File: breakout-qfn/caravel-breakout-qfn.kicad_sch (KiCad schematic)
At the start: 16 parts, among them CON1 REF-182665-01, CON2 REF-182665-01, CON3 73251-1352, U1 Caravel_QFN, U2 TLV73318PDBV

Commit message: v2.0
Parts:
- removed C8, C9: 0.1uf, Capacitor_SMD:C_0603_1608Metric, symbol Device:C
- removed U2: TLV73318PDBV, Package_TO_SOT_SMD:SOT-23-5, symbol Regulator_Linear:TLV73318PDBV
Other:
- title: (none) -> Caravel QFN Breakout
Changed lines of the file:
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@@
 (kicad_sch (version 20230121) (generator eeschema)
   (paper "A")
+  (title_block
+    (title "Caravel QFN Breakout")
+    (date "2023-07-17")
+    (rev "2.0")
+  )
   (junction (at 41.91 93.98) (diameter 0) (color 0 0 0 0)
   )
@@
     )
   )
-  (symbol (lib_id "Device:C") (at 161.29 156.21 180) (unit 1)
-    (in_bom yes) (on_board yes) (dnp no)
-    (property "Reference" "C9" (at 157.48 156.21 90)
-      (effects (font (size 1.27 1.27)))
-    )
-    (property "Value" "0.1uf" (at 154.94 156.21 90)
-      (effects (font (size 1.27 1.27)))
-    )
-    (property "Footprint" "Capacitor_SMD:C_0603_1608Metric" (at 160.3248 152.4 0)
-      (effects (font (size 1.27 1.27)) hide)
-    )
-    (property "Datasheet" "~" (at 161.29 156.21 0)
-      (effects (font (size 1.27 1.27)) hide)
-    )
-    (pin "1")
-    (pin "2")
-    (instances
-      (project "caravel-breakout-qfn"
-        (path "/b38c65ac-2d57-46f9-9a32-ad09573ee400"
-          (reference "C9") (unit 1)
-        )
-      )
-    )
-  )
-  (symbol (lib_id "Regulator_Linear:TLV73318PDBV") (at 146.05 154.94 0) (unit 1)
-    (in_bom yes) (on_board yes) (dnp no) (fields_autoplaced)
-    (property "Reference" "U2" (at 146.05 144.78 0)
-      (effects (font (size 1.27 1.27)))
-    )
-    (property "Value" "TLV73318PDBV" (at 146.05 147.32 0)
-      (effects (font (size 1.27 1.27)))
-    )
-    (property "Footprint" "Package_TO_SOT_SMD:SOT-23-5" (at 146.05 146.685 0)
-      (effects (font (size 1.27 1.27) italic) hide)
-    )
-    (property "Datasheet" "http://www.ti.com/lit/ds/symlink/tlv733p.pdf" (at 146.05 154.94 0)
-      (effects (font (size 1.27 1.27)) hide)
-    )
-    (pin "1")
-    (pin "2")
-    (pin "3")
-    (pin "4")
-    (pin "5")
-    (instances
-      (project "caravel-breakout-qfn"
-        (path "/b38c65ac-2d57-46f9-9a32-ad09573ee400"
-          (reference "U2") (unit 1)
-        )
-      )
-    )
-  )
   (symbol (lib_id "power:GND") (at 72.39 114.3 0) (unit 1)
     (in_bom yes) (on_board yes) (dnp no)
@@
         )
       )
-    )
-  )
-  (symbol (lib_id "Device:C") (at 130.81 156.21 180) (unit 1)
-    (in_bom yes) (on_board yes) (dnp no)
-    (property "Reference" "C8" (at 127 156.21 90)
-      (effects (font (size 1.27 1.27)))
-    )
-    (property "Value" "0.1uf" (at 124.46 156.21 90)
-      (effects (font (size 1.27 1.27)))
-    )
-    (property "Footprint" "Capacitor_SMD:C_0603_1608Metric" (at 129.8448 152.4 0)
-      (effects (font (size 1.27 1.27)) hide)
-    )
-    (property "Datasheet" "~" (at 130.81 156.21 0)
-      (effects (font (size 1.27 1.27)) hide)
-    )
-    (pin "1")
-    (pin "2")
-    (instances
-      (project "caravel-breakout-qfn"
-        (path "/b38c65ac-2d57-46f9-9a32-ad09573ee400"
-          (reference "C8") (unit 1)
-        )
-      )

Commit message: QFN breakout v2.1: fixes to footprint s.masks, cleanup, flipped logos
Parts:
- CON1, CON2: footprint ok-connectors:REF-182665-01 -> BreakoutCommon:REF-182665-01
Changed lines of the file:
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@@
   (title_block
     (title "Caravel QFN Breakout")
-    (date "2023-07-17")
-    (rev "2.0")
+    (date "2023-07-21")
+    (rev "2.1")
   )
   (junction (at 41.91 93.98) (diameter 0) (color 0 0 0 0)
@@
       (effects (font (size 1.27 1.27)))
     )
-    (property "Footprint" "ok-connectors:REF-182665-01" (at 222.25 52.07 0)
+    (property "Footprint" "BreakoutCommon:REF-182665-01" (at 222.25 52.07 0)
       (effects (font (size 1.27 1.27)) hide)
     )
@@
       (effects (font (size 1.27 1.27)))
     )
-    (property "Footprint" "ok-connectors:REF-182665-01" (at 222.25 125.73 0)
-      (effects (font (size 1.27 1.27)) hide)
-    )
+    (property "Footprint" "BreakoutCommon:REF-182665-01" (at 222.25 125.73 0)
+      (effects (font (size 1.27 1.27)) hide)
+    )

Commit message: QFN v2.2, using cheaper FH-00339 headers
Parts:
- CON1, CON2: footprint BreakoutCommon:REF-182665-01 -> BreakoutCommon:FH-00339
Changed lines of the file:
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@@
       (effects (font (size 1.27 1.27)))
     )
-    (property "Footprint" "BreakoutCommon:REF-182665-01" (at 222.25 52.07 0)
+    (property "Footprint" "BreakoutCommon:FH-00339" (at 222.25 52.07 0)
       (effects (font (size 1.27 1.27)) hide)
     )
@@
       (effects (font (size 1.27 1.27)))
     )
-    (property "Footprint" "BreakoutCommon:REF-182665-01" (at 222.25 125.73 0)
-      (effects (font (size 1.27 1.27)) hide)
-    )
+    (property "Footprint" "BreakoutCommon:FH-00339" (at 222.25 125.73 0)
+      (effects (font (size 1.27 1.27)) hide)
+    )

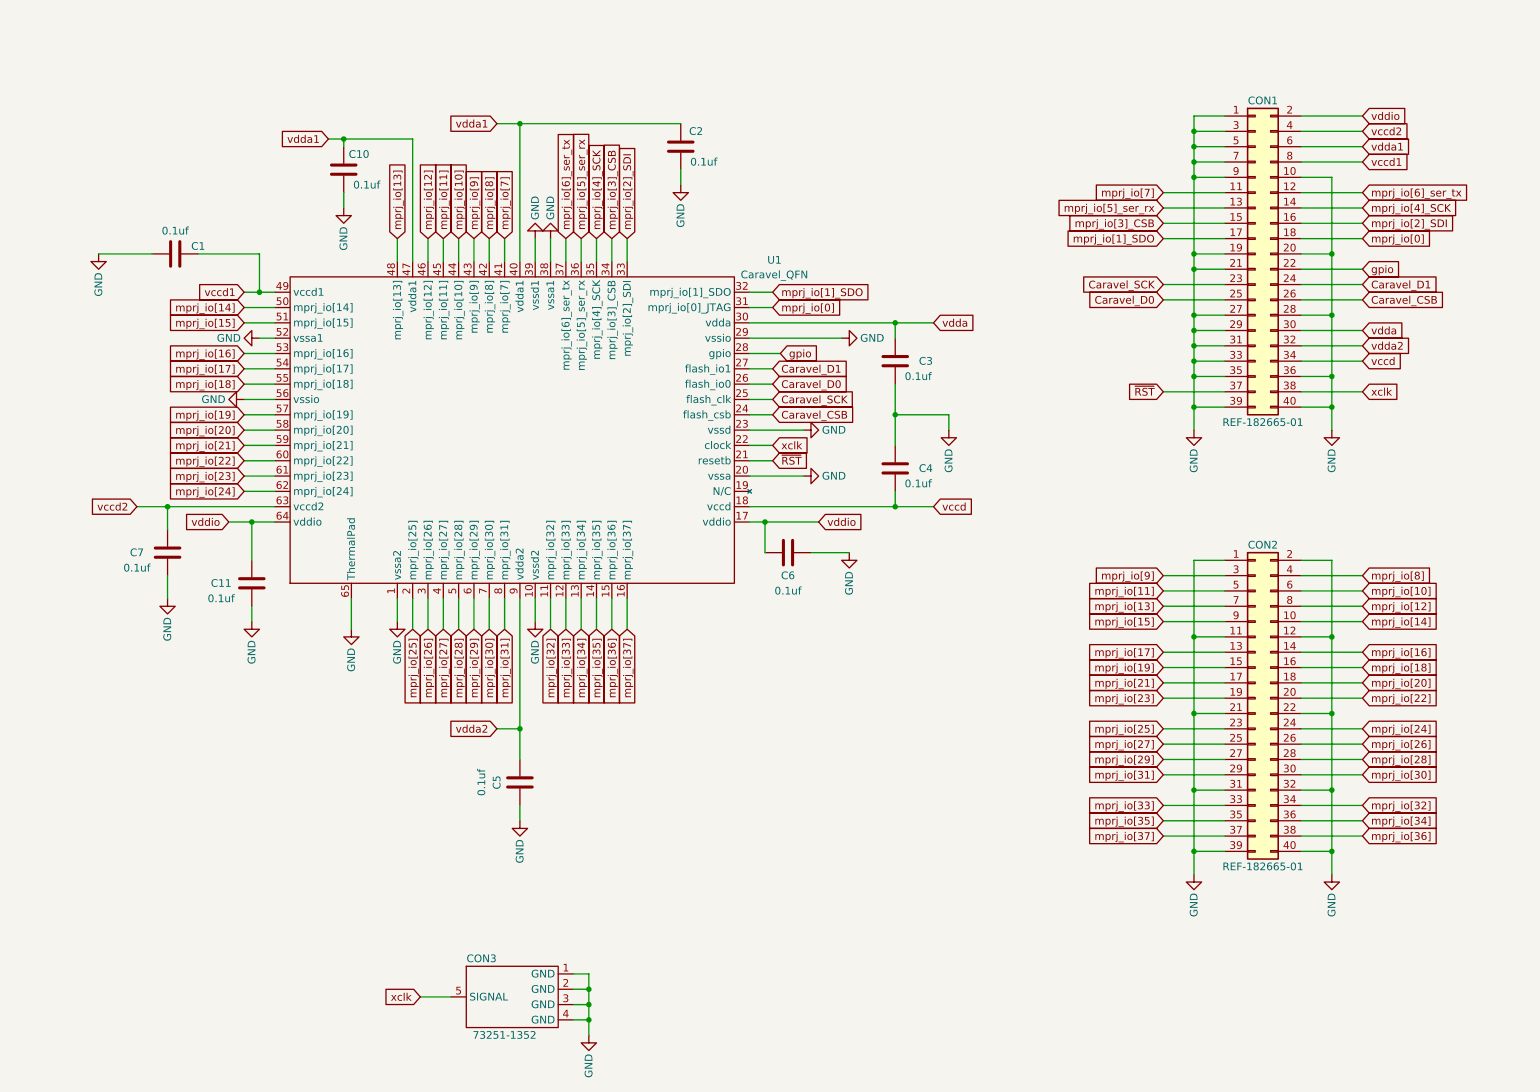
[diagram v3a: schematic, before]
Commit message: QFN breakout sanity naming for nets
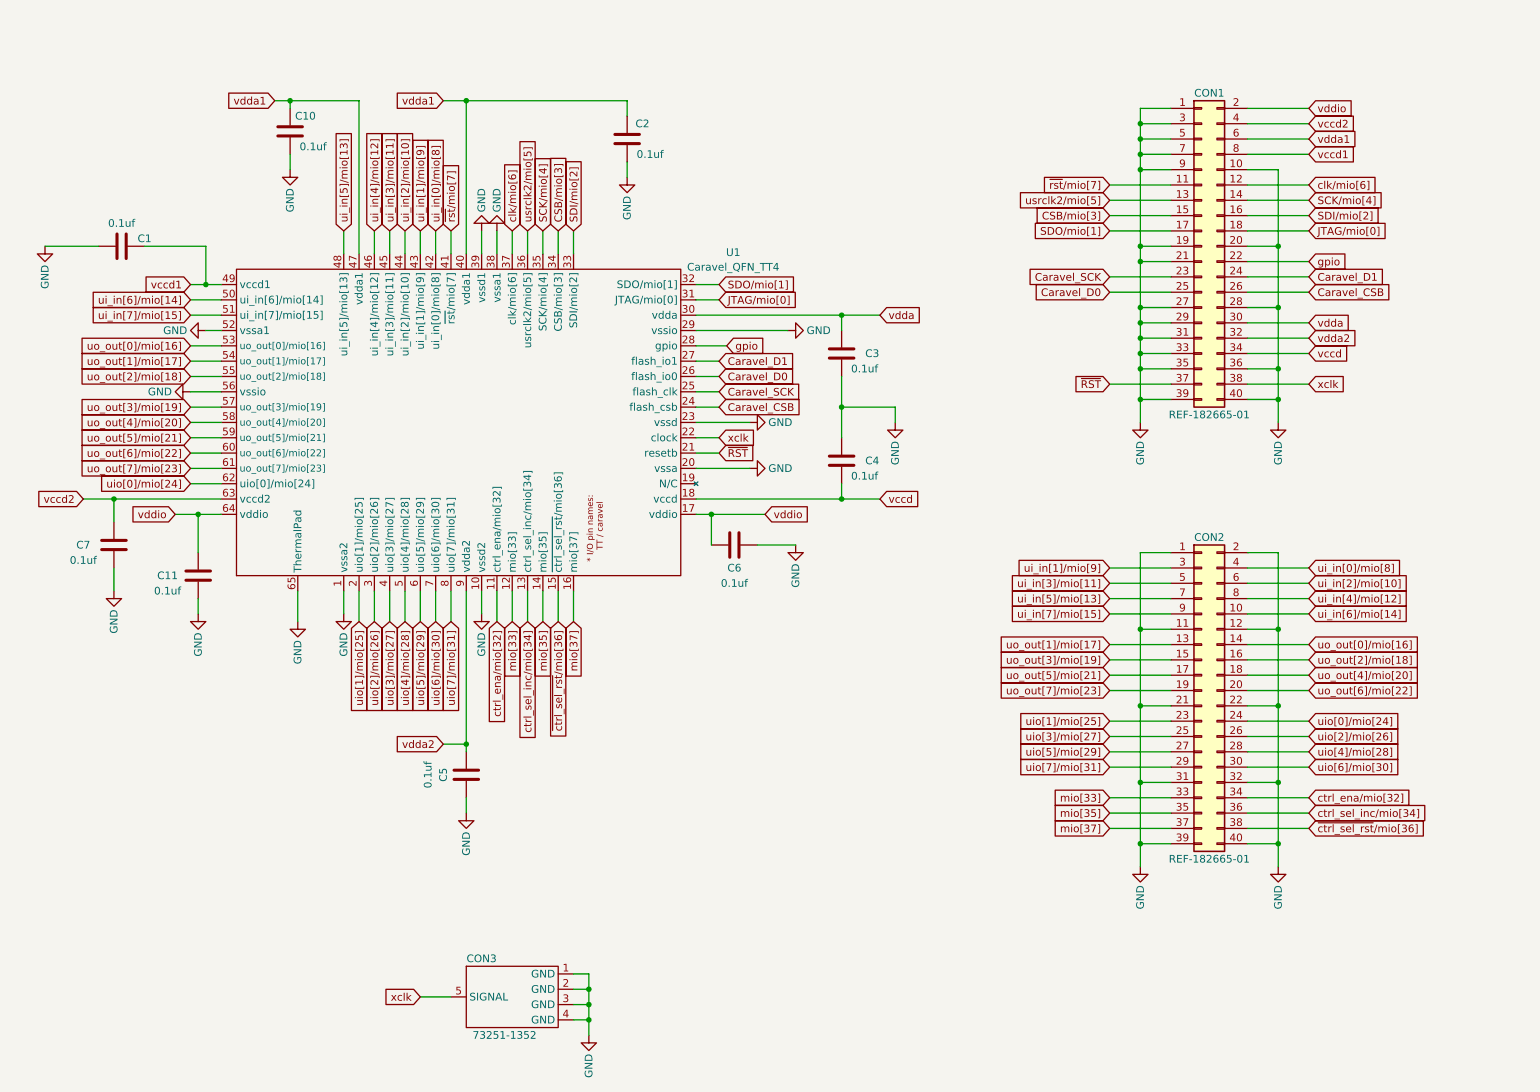
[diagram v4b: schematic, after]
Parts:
- removed U1: Caravel_QFN, Package_DFN_QFN:QFN-64-1EP_9x9mm_P0.5mm_EP7.65x7.65mm, symbol CaravelCommon:Caravel_QFN
- added U1: Caravel_QFN_TT4, TinyTapeout:QFN-64-1EP_9x9mm_P0.5mm_EP7.65x7.65mm_REDUCEDPASTE, symbol TinyTapeout:Caravel_QFN_TT4
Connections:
- net Caravel_CSB: now also U1.24 (flash_csb)
- net Caravel_D0: now also U1.26 (flash_io0)
- net Caravel_D1: now also U1.27 (flash_io1)
- net Caravel_SCK: now also U1.25 (flash_clk)
- net GND: now also U1.1 (vssa2), U1.10 (vssd2), U1.20 (vssa), U1.23 (vssd), U1.29 (vssio), U1.38 (vssa1), U1.39 (vssd1), U1.52 (vssa1), U1.56 (vssio), U1.65 (ThermalPad)
- net gpio: now also U1.28 (gpio)
- net vccd: now also U1.18 (vccd)
- net vccd1: now also U1.49 (vccd1)
- net vccd2: now also U1.63 (vccd2)
- net vdda: now also U1.30 (vdda)
- net vdda1: now also U1.40 (vdda1), U1.47 (vdda1)
- net vdda2: now also U1.9 (vdda2)
- net vddio: now also U1.17 (vddio), U1.64 (vddio)
- net xclk: now also U1.22 (clock)
- net ~{RST}: now also U1.21 (resetb)
- net mprj_io[0] renamed JTAG/mio[0]
- net JTAG/mio[0]: now also U1.31 (JTAG/mio[0])
- net mprj_io[10] renamed ui_in[2]/mio[10]
- net ui_in[2]/mio[10]: now also U1.44 (ui_in[2]/mio[10])
- net mprj_io[11] renamed ui_in[3]/mio[11]
- net ui_in[3]/mio[11]: now also U1.45 (ui_in[3]/mio[11])
- net mprj_io[12] renamed ui_in[4]/mio[12]
- net ui_in[4]/mio[12]: now also U1.46 (ui_in[4]/mio[12])
- net mprj_io[13] renamed ui_in[5]/mio[13]
- net ui_in[5]/mio[13]: now also U1.48 (ui_in[5]/mio[13])
- net mprj_io[14] renamed ui_in[6]/mio[14]
- net ui_in[6]/mio[14]: now also U1.50 (ui_in[6]/mio[14])
- net mprj_io[15] renamed ui_in[7]/mio[15]
- net ui_in[7]/mio[15]: now also U1.51 (ui_in[7]/mio[15])
- net mprj_io[16] renamed uo_out[0]/mio[16]
- net uo_out[0]/mio[16]: now also U1.53 (uo_out[0]/mio[16])
- net mprj_io[17] renamed uo_out[1]/mio[17]
- net uo_out[1]/mio[17]: now also U1.54 (uo_out[1]/mio[17])
- net mprj_io[18] renamed uo_out[2]/mio[18]
- net uo_out[2]/mio[18]: now also U1.55 (uo_out[2]/mio[18])
- net mprj_io[19] renamed uo_out[3]/mio[19]
- net uo_out[3]/mio[19]: now also U1.57 (uo_out[3]/mio[19])
- net mprj_io[1]_SDO renamed SDO/mio[1]
- net SDO/mio[1]: now also U1.32 (SDO/mio[1])
- net mprj_io[20] renamed uo_out[4]/mio[20]
- net uo_out[4]/mio[20]: now also U1.58 (uo_out[4]/mio[20])
- net mprj_io[21] renamed uo_out[5]/mio[21]
- net uo_out[5]/mio[21]: now also U1.59 (uo_out[5]/mio[21])
- net mprj_io[22] renamed uo_out[6]/mio[22]
- net uo_out[6]/mio[22]: now also U1.60 (uo_out[6]/mio[22])
- net mprj_io[23] renamed uo_out[7]/mio[23]
- net uo_out[7]/mio[23]: now also U1.61 (uo_out[7]/mio[23])
- net mprj_io[24] renamed uio[0]/mio[24]
- net uio[0]/mio[24]: now also U1.62 (uio[0]/mio[24])
- net mprj_io[25] renamed uio[1]/mio[25]
- net uio[1]/mio[25]: now also U1.2 (uio[1]/mio[25])
- net mprj_io[26] renamed uio[2]/mio[26]
- net uio[2]/mio[26]: now also U1.3 (uio[2]/mio[26])
- net mprj_io[27] renamed uio[3]/mio[27]
- net uio[3]/mio[27]: now also U1.4 (uio[3]/mio[27])
- net mprj_io[28] renamed uio[4]/mio[28]
- net uio[4]/mio[28]: now also U1.5 (uio[4]/mio[28])
- net mprj_io[29] renamed uio[5]/mio[29]
- net uio[5]/mio[29]: now also U1.6 (uio[5]/mio[29])
- net mprj_io[2]_SDI renamed SDI/mio[2]
- net SDI/mio[2]: now also U1.33 (SDI/mio[2])
- net mprj_io[30] renamed uio[6]/mio[30]
- net uio[6]/mio[30]: now also U1.7 (uio[6]/mio[30])
- net mprj_io[31] renamed uio[7]/mio[31]
- net uio[7]/mio[31]: now also U1.8 (uio[7]/mio[31])
- net mprj_io[32] renamed ctrl_ena/mio[32]
- net ctrl_ena/mio[32]: now also U1.11 (ctrl_ena/mio[32])
- net mprj_io[33] renamed mio[33]
- net mio[33]: now also U1.12 (mio[33])
- net mprj_io[34] renamed ctrl_sel_inc/mio[34]
- net ctrl_sel_inc/mio[34]: now also U1.13 (ctrl_sel_inc/mio[34])
- net mprj_io[35] renamed mio[35]
- net mio[35]: now also U1.14 (mio[35])
- net mprj_io[36] renamed ~{ctrl_sel_rst}/mio[36]
- net ~{ctrl_sel_rst}/mio[36]: now also U1.15 (~{ctrl_sel_rst}/mio[36])
- net mprj_io[37] renamed mio[37]
- net mio[37]: now also U1.16 (mio[37])
- net mprj_io[3]_CSB renamed CSB/mio[3]
- net CSB/mio[3]: now also U1.34 (CSB/mio[3])
- net mprj_io[4]_SCK renamed SCK/mio[4]
- net SCK/mio[4]: now also U1.35 (SCK/mio[4])
- net mprj_io[5]_ser_rx renamed usrclk2/mio[5]
- net usrclk2/mio[5]: now also U1.36 (usrclk2/mio[5])
- net mprj_io[6]_ser_tx renamed clk/mio[6]
- net clk/mio[6]: now also U1.37 (clk/mio[6])
- net mprj_io[7] renamed ~{rst}/mio[7]
- net ~{rst}/mio[7]: now also U1.41 (~{rst}/mio[7])
- net mprj_io[8] renamed ui_in[0]/mio[8]
- net ui_in[0]/mio[8]: now also U1.42 (ui_in[0]/mio[8])
- net mprj_io[9] renamed ui_in[1]/mio[9]
- net ui_in[1]/mio[9]: now also U1.43 (ui_in[1]/mio[9])
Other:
- moved on the sheet: C1, C10, C11, C2, C3, C4, C5, C6, C7, CON1, CON2
